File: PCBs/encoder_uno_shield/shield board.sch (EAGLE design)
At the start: 11 parts, among them U1 ARDUINOR3-BPLACE

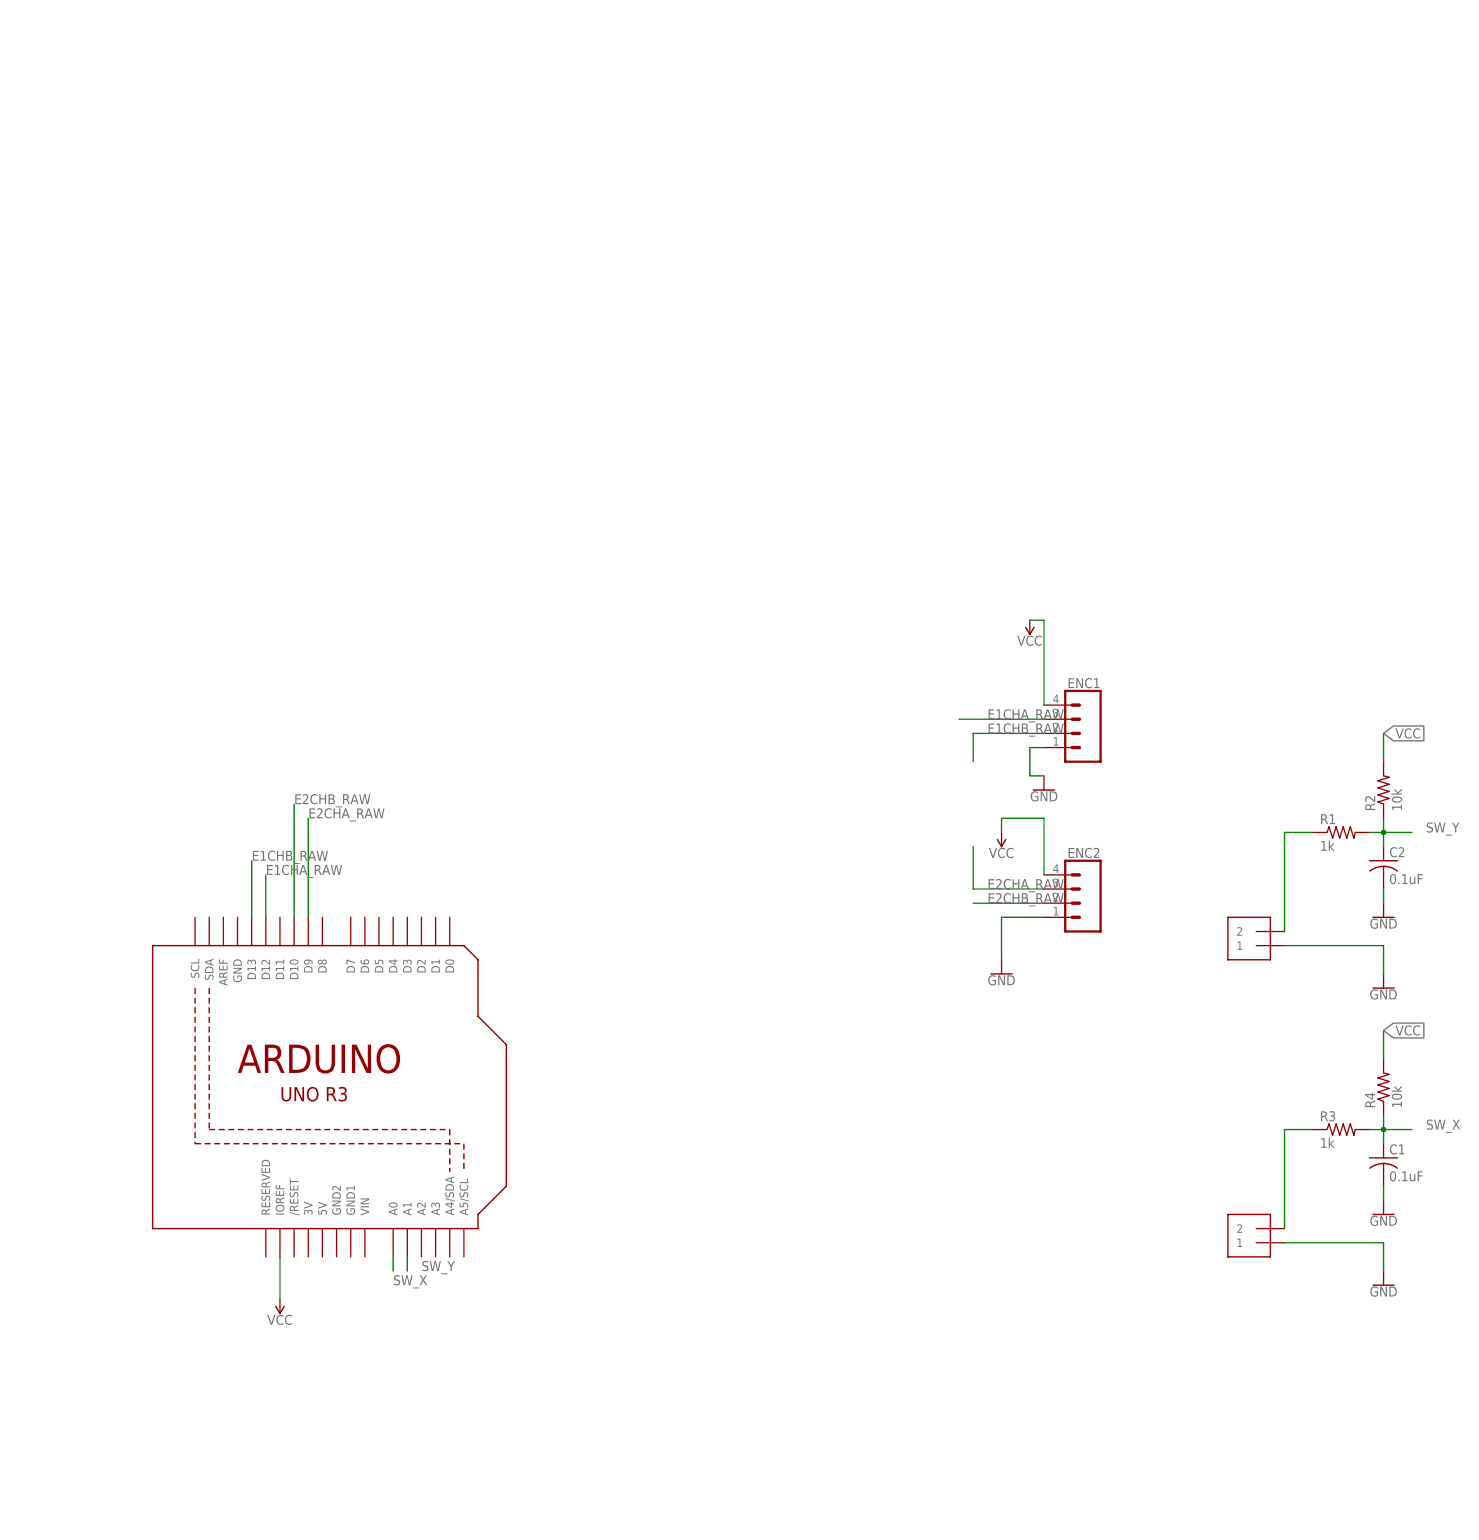
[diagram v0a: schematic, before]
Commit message: added debounce to sch, about to delete and add back as design block
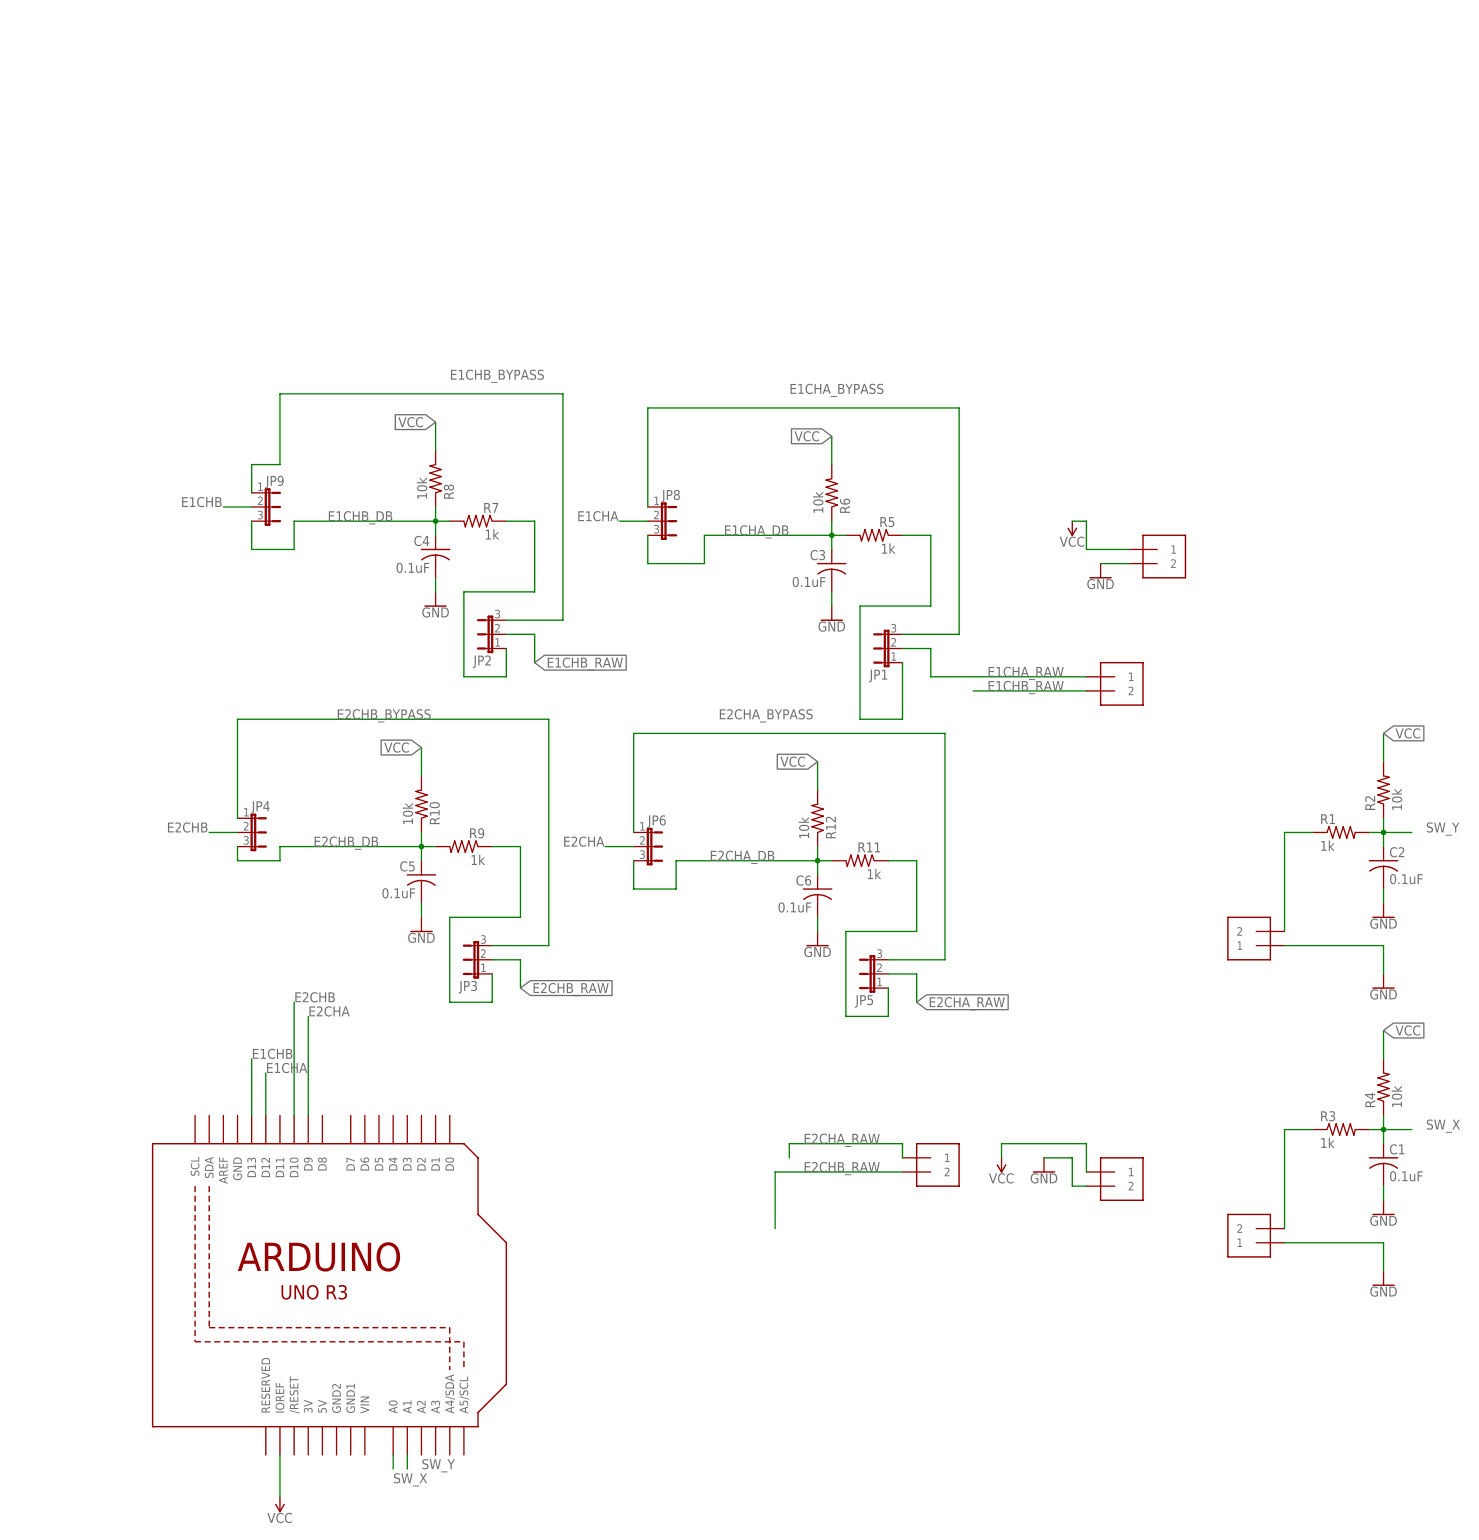
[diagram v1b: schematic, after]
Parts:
- removed ENC1, ENC2: (no value), SparkFun-Connectors:CONN_04JST-PTH
- added C3, C4, C5, C6: 0.1uF, adafruit:C-USC0603
- added JP1, JP2, JP3, JP4, JP5, JP6, JP8, JP9: (no value), jumper:JP2E
- added R10, R12, R6, R8: 10k, resistor:R-US_R0603
- added R11, R5, R7, R9: 1k, resistor:R-US_R0603
- added U$3, U$4, U$5, U$6: MOLEX_0039301022, pat:MOLEX_0039301022
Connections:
- new net E1CHA: JP8.2, U1.D12
- new net E1CHA_BYPASS: JP1.3, JP8.1
- new net E1CHA_DB: C3.1, JP8.3, R5.2, R6.1
- new net E1CHB: JP9.2, U1.D13
- new net E1CHB_BYPASS: JP2.3, JP9.1
- new net E1CHB_DB: C4.1, JP9.3, R7.2, R8.1
- new net E2CHA: JP6.2, U1.D9
- new net E2CHA_BYPASS: JP5.3, JP6.1
- new net E2CHA_DB: C6.1, JP6.3, R11.2, R12.1
- new net E2CHB: JP4.2, U1.D10
- new net E2CHB_BYPASS: JP3.3, JP4.1
- new net E2CHB_DB: C5.1, JP4.3, R10.1, R9.2
- new net N$2: JP1.1, R5.1
- new net N$3: JP2.1, R7.1
- new net N$5: JP3.1, R9.1
- new net N$6: JP5.1, R11.1
- net E1CHA_RAW: now also JP1.2, U$5.1; no longer ENC1.3, U1.D12
- net E1CHB_RAW: now also JP2.2, U$5.2; no longer ENC1.2, U1.D13
- net E2CHA_RAW: now also JP5.2, U$6.1; no longer ENC2.3, U1.D9
- net E2CHB_RAW: now also JP3.2, U$6.2; no longer ENC2.2, U1.D10
- net GND: now also C3.2, C4.2, C5.2, C6.2, U$3.2, U$4.2; no longer ENC1.1, ENC2.1
- net VCC: now also R10.2, R12.2, R6.2, R8.2, U$3.1, U$4.1; no longer ENC1.4, ENC2.4

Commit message: jumper togglable debounce circuit added for encoders
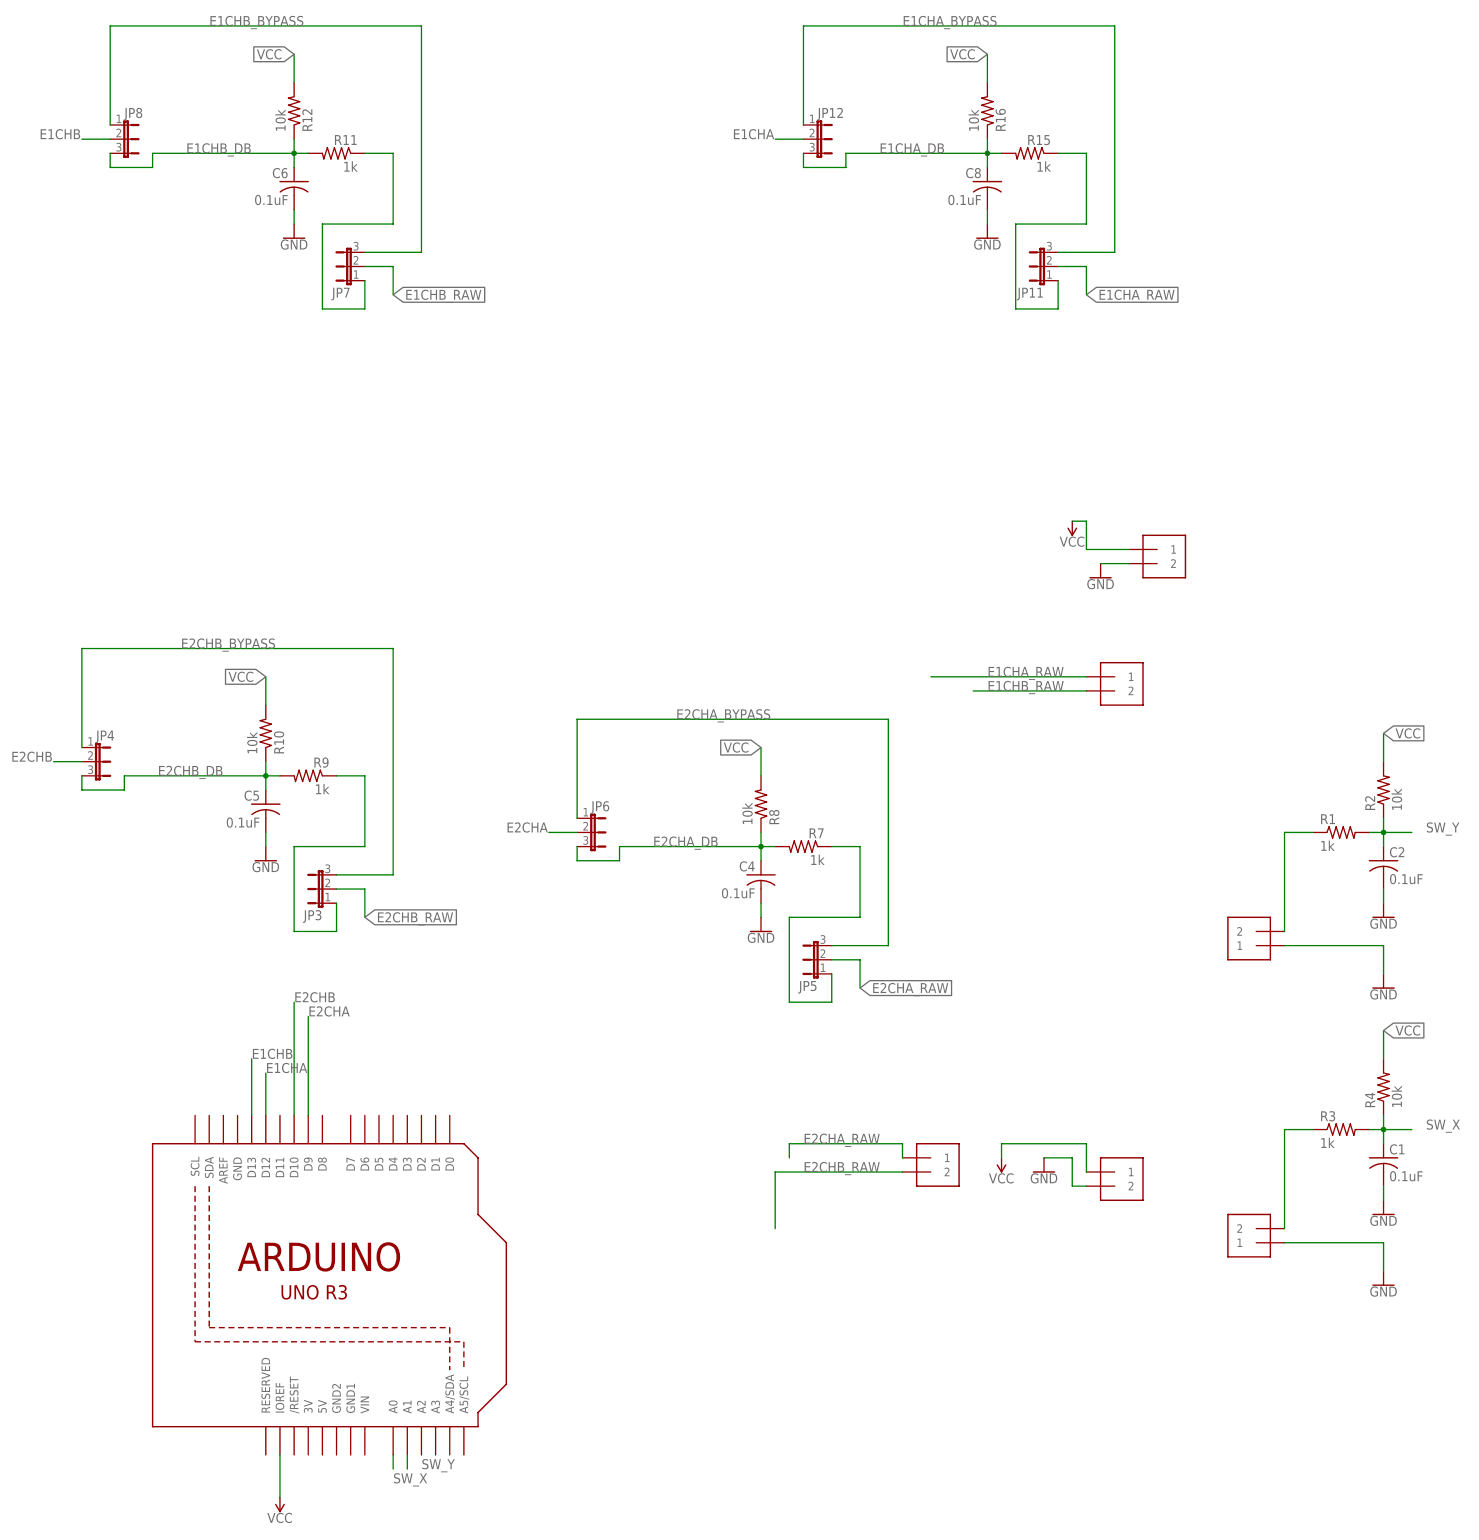
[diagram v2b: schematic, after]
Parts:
- removed C3: 0.1uF, adafruit:C-USC0603
- removed JP1, JP2, JP9: (no value), jumper:JP2E
- removed R5: 1k, resistor:R-US_R0603
- removed R6: 10k, resistor:R-US_R0603
- added C8: 0.1uF, adafruit:C-USC0603
- added JP11, JP12, JP7: (no value), jumper:JP2E
- added R15: 1k, resistor:R-US_R0603
- added R16: 10k, resistor:R-US_R0603
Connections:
- removed net N$2: JP1.1, R5.1
- new net N$8: JP11.1, R15.1
- net E1CHA: now also JP12.2; no longer JP8.2
- net E1CHA_BYPASS: now also JP11.3, JP12.1; no longer JP1.3, JP8.1
- net E1CHA_DB: now also C8.1, JP12.3, R15.2, R16.1; no longer C3.1, JP8.3, R5.2, R6.1
- net E1CHA_RAW: now also JP11.2; no longer JP1.2
- net E1CHB: now also JP8.2; no longer JP9.2
- net E1CHB_BYPASS: now also JP7.3, JP8.1; no longer JP2.3, JP9.1
- net E1CHB_DB: now also C6.1, JP8.3, R11.2, R12.1; no longer C4.1, JP9.3, R7.2, R8.1
- net E1CHB_RAW: now also JP7.2; no longer JP2.2
- net E2CHA_DB: now also C4.1, R7.2, R8.1; no longer C6.1, R11.2, R12.1
- net GND: now also C8.2; no longer C3.2
- net N$3: now also JP5.1; no longer JP2.1
- net N$6: now also JP7.1; no longer JP5.1
- net VCC: now also R16.2; no longer R6.2
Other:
- moved on the sheet: C4, C5, C6, JP3, JP4, JP5, JP6, JP8, R10, R11, R12, R7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
